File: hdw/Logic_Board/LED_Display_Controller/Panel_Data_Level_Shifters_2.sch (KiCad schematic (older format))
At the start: 62 parts, among them U2701 74HCT541, U2702 74HCT541

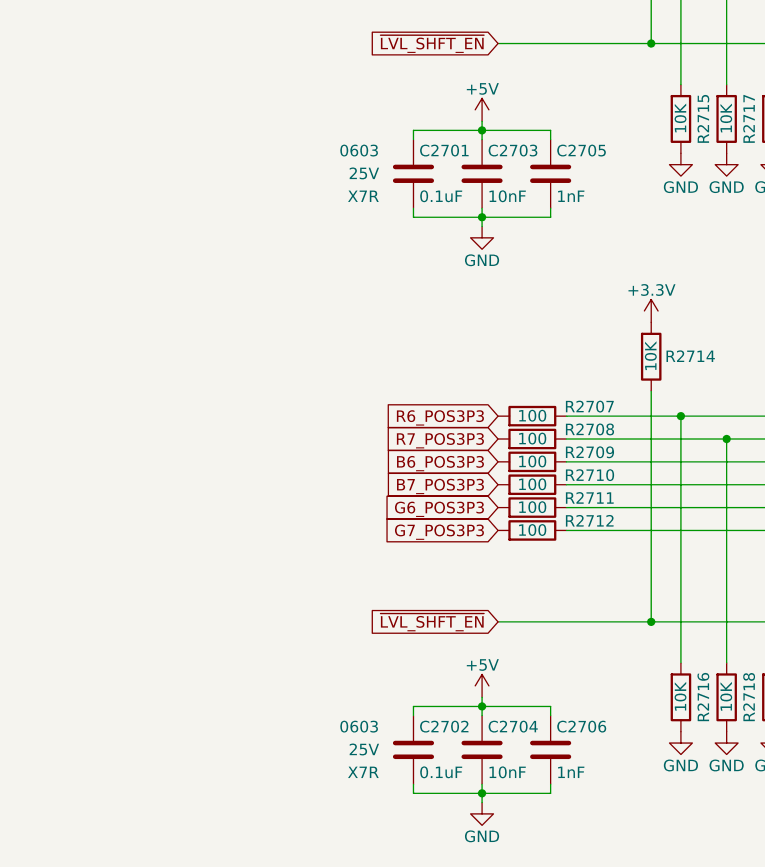
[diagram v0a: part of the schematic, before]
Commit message: Added some digikey partnumbers to components
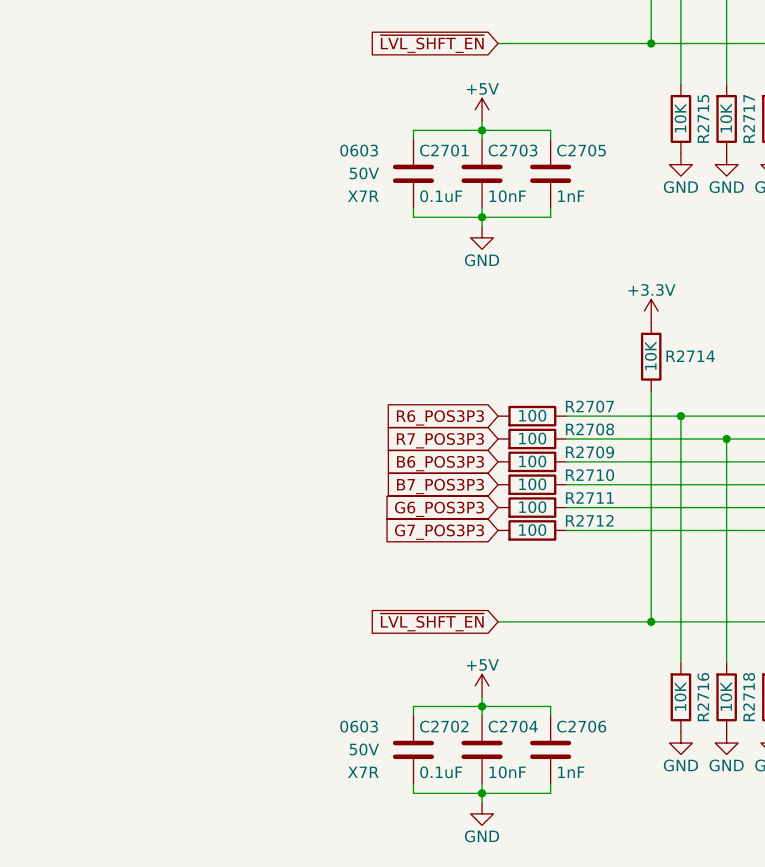
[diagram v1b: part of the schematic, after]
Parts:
- C2701, C2702: footprint (none) -> Capacitors_SMD:C_0603; Digi-Key PN PN -> 311-1344-1-ND; Voltage 25V -> 50V
- C2703, C2704: Digi-Key PN PN -> 1276-1921-1-ND; Voltage 25V -> 50V
- C2705, C2706: Digi-Key PN PN -> 1276-1018-1-ND; Voltage 25V -> 50V
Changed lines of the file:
@@
 F 0 "C2701" H 2305 3290 50  0000 L CNN
 F 1 "0.1uF" H 2305 3090 50  0000 L CNN
-F 2 "" H 2318 3040 50  0001 C CNN
+F 2 "Capacitors_SMD:C_0603" H 2318 3040 50  0001 C CNN
 F 3 "" H 2305 3290 50  0001 C CNN
 F 4 "0603" H 2130 3290 50  0000 R CNN "display_footprint"
-F 5 "25V" H 2130 3190 50  0000 R CNN "Voltage"
+F 5 "50V" H 2130 3190 50  0000 R CNN "Voltage"
 F 6 "X7R" H 2130 3090 50  0000 R CNN "Dielectric"
-F 7 "PN" H 2705 3690 60  0001 C CNN "Digi-Key PN"
+F 7 "311-1344-1-ND" H 2705 3690 60  0001 C CNN "Digi-Key PN"
 	1    2280 3190
 	1    0    0    -1
@@
 F 3 "" H 2605 3290 50  0001 C CNN
 F 4 "0603" H 2430 3290 50  0001 R CNN "display_footprint"
-F 5 "25V" H 2430 3190 50  0001 R CNN "Voltage"
+F 5 "50V" H 2430 3190 50  0001 R CNN "Voltage"
 F 6 "X7R" H 2430 3090 50  0001 R CNN "Dielectric"
-F 7 "PN" H 3005 3690 60  0001 C CNN "Digi-Key PN"
+F 7 "1276-1921-1-ND" H 3005 3690 60  0001 C CNN "Digi-Key PN"
 	1    2580 3190
 	1    0    0    -1
@@
 F 3 "" H 2905 3290 50  0001 C CNN
 F 4 "0603" H 2730 3290 50  0001 R CNN "display_footprint"
-F 5 "25V" H 2730 3190 50  0001 R CNN "Voltage"
+F 5 "50V" H 2730 3190 50  0001 R CNN "Voltage"
 F 6 "X7R" H 2730 3090 50  0001 R CNN "Dielectric"
-F 7 "PN" H 3305 3690 60  0001 C CNN "Digi-Key PN"
+F 7 "1276-1018-1-ND" H 3305 3690 60  0001 C CNN "Digi-Key PN"
 	1    2880 3190
 	1    0    0    -1
@@
 F 0 "C2702" H 2305 5810 50  0000 L CNN
 F 1 "0.1uF" H 2305 5610 50  0000 L CNN
-F 2 "" H 2318 5560 50  0001 C CNN
+F 2 "Capacitors_SMD:C_0603" H 2318 5560 50  0001 C CNN
 F 3 "" H 2305 5810 50  0001 C CNN
 F 4 "0603" H 2130 5810 50  0000 R CNN "display_footprint"
-F 5 "25V" H 2130 5710 50  0000 R CNN "Voltage"
+F 5 "50V" H 2130 5710 50  0000 R CNN "Voltage"
 F 6 "X7R" H 2130 5610 50  0000 R CNN "Dielectric"
-F 7 "PN" H 2705 6210 60  0001 C CNN "Digi-Key PN"
+F 7 "311-1344-1-ND" H 2705 6210 60  0001 C CNN "Digi-Key PN"
 	1    2280 5710
 	1    0    0    -1
@@
 F 3 "" H 2605 5810 50  0001 C CNN
 F 4 "0603" H 2430 5810 50  0001 R CNN "display_footprint"
-F 5 "25V" H 2430 5710 50  0001 R CNN "Voltage"
+F 5 "50V" H 2430 5710 50  0001 R CNN "Voltage"
 F 6 "X7R" H 2430 5610 50  0001 R CNN "Dielectric"
-F 7 "PN" H 3005 6210 60  0001 C CNN "Digi-Key PN"
+F 7 "1276-1921-1-ND" H 3005 6210 60  0001 C CNN "Digi-Key PN"
 	1    2580 5710
 	1    0    0    -1
@@
 F 3 "" H 2905 5810 50  0001 C CNN
 F 4 "0603" H 2730 5810 50  0001 R CNN "display_footprint"
-F 5 "25V" H 2730 5710 50  0001 R CNN "Voltage"
+F 5 "50V" H 2730 5710 50  0001 R CNN "Voltage"
 F 6 "X7R" H 2730 5610 50  0001 R CNN "Dielectric"
-F 7 "PN" H 3305 6210 60  0001 C CNN "Digi-Key PN"
+F 7 "1276-1018-1-ND" H 3305 6210 60  0001 C CNN "Digi-Key PN"
 	1    2880 5710
 	1    0    0    -1

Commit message: Finished first pass of digikey part numbers
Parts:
- R2701, R2702, R2703, R2704, R2705, R2706, R2707, R2708, R2709, R2710, R2711, R2712, R2743, R2744, R2745, R2746, R2747, R2748, R2749, R2750, R2751, R2752, R2753, R2754: Digi-Key PN PN -> A106047CT-ND
- R2713, R2714, R2715, R2716, R2717, R2718, R2719, R2720, R2721, R2722, R2723, R2724, R2725, R2726, R2727, R2728, R2729, R2730, R2731, R2732, R2733, R2734, R2735, R2736, R2737, R2738, R2739, R2740, R2741, R2742: Digi-Key PN PN -> RMCF0603FT10K0CT-ND
- U2701, U2702: Digi-Key PN (none) -> 296-26499-1-ND

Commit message: First pass assignment of footprints to all components
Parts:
- C2703, C2704, C2705, C2706: footprint (none) -> Capacitors_SMD:C_0603
- R2701, R2702, R2703, R2704, R2705, R2706, R2707, R2708, R2709, R2710, R2711, R2712, R2713, R2714, R2715, R2716, R2717, R2718, R2719, R2720, R2721, R2722, R2723, R2724, R2725, R2726, R2727, R2728, R2729, R2730, R2731, R2732, R2733, R2734, R2735, R2736, R2737, R2738, R2739, R2740, R2741, R2742, R2743, R2744, R2745, R2746, R2747, R2748, R2749, R2750, R2751, R2752, R2753, R2754: footprint (none) -> Resistors_SMD:R_0603
- U2701, U2702: footprint (none) -> Housings_SSOP:TSSOP-20_4.4x6.5mm_Pitch0.65mm

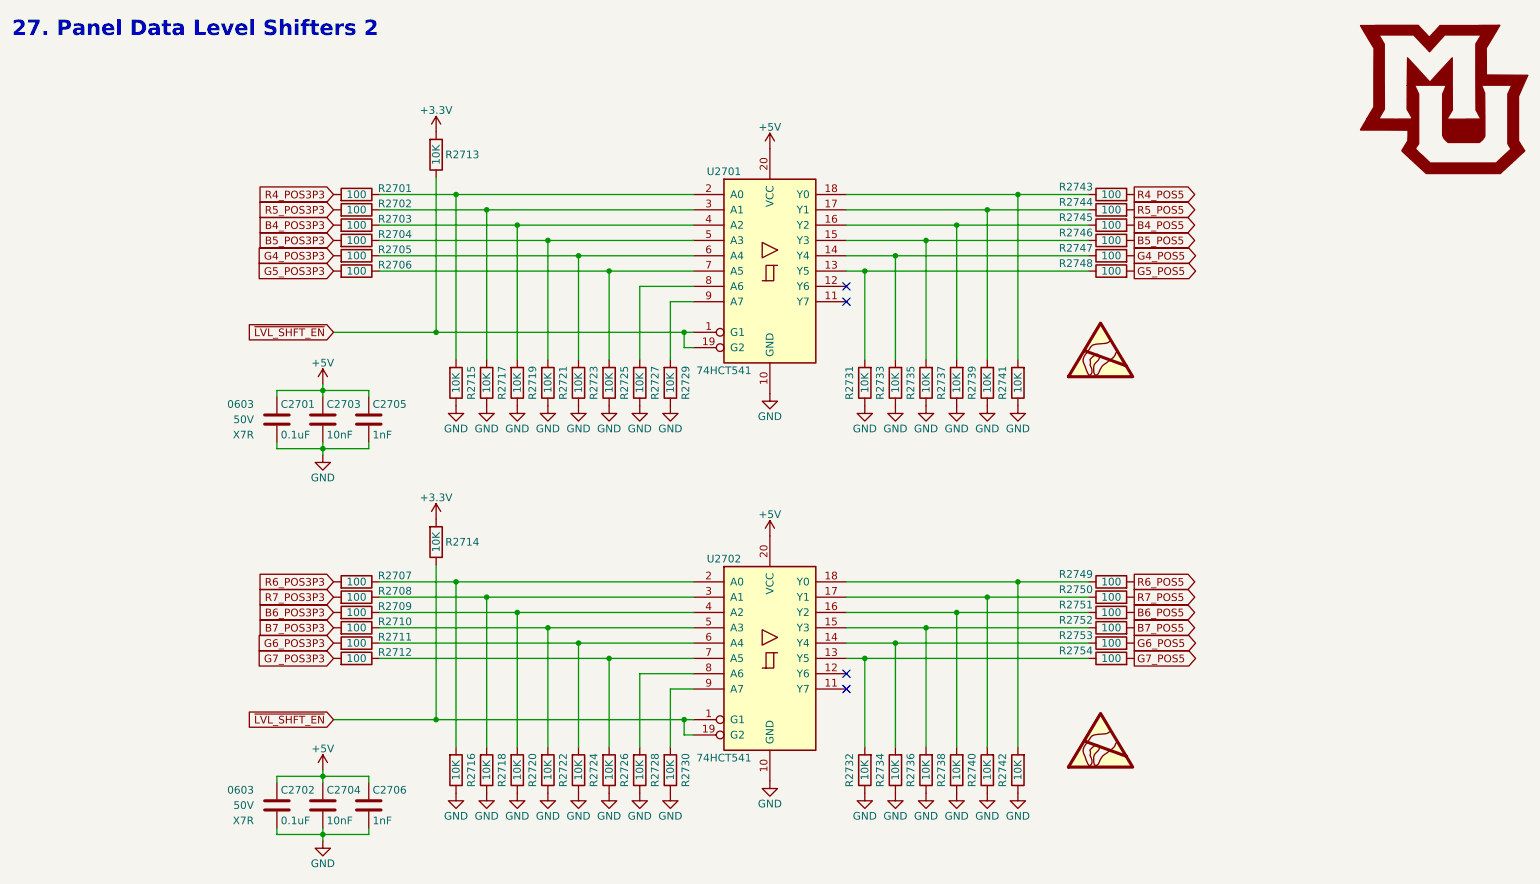
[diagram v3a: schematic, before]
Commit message: Fixed net placement on level shifters, lots of part placements on PCB
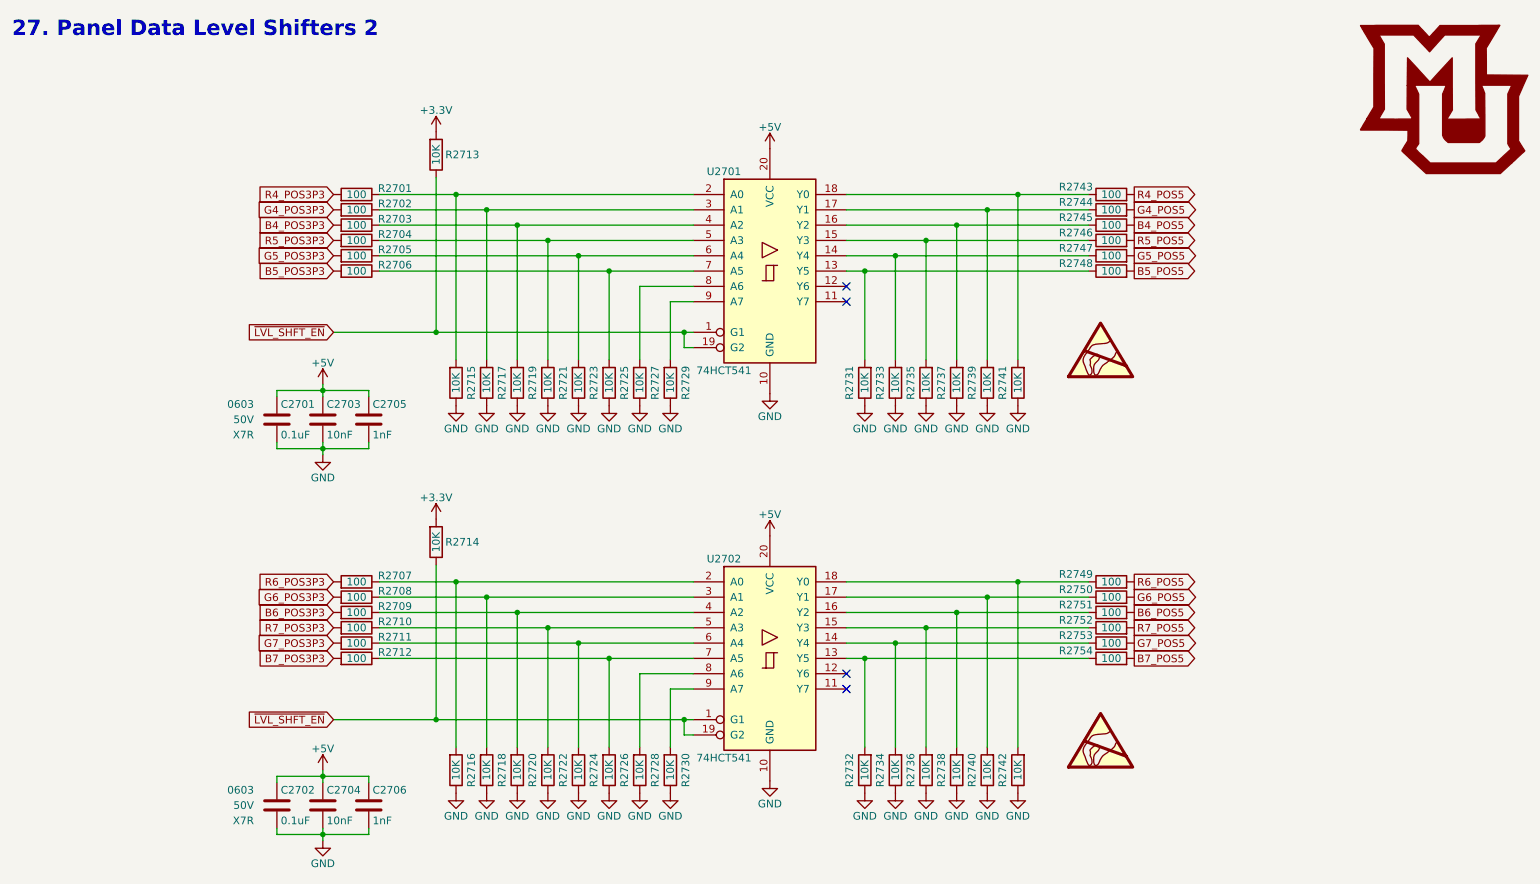
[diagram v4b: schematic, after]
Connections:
- net B5_POS3P3: now also R2706.1; no longer R2704.1
- net B5_POS5: now also R2748.1; no longer R2746.1
- net B7_POS3P3: now also R2712.1; no longer R2710.1
- net B7_POS5: now also R2754.1; no longer R2752.1
- net G4_POS3P3: now also R2702.1; no longer R2705.1
- net G4_POS5: now also R2744.1; no longer R2747.1
- net G5_POS3P3: now also R2705.1; no longer R2706.1
- net G5_POS5: now also R2747.1; no longer R2748.1
- net G6_POS3P3: now also R2708.1; no longer R2711.1
- net G6_POS5: now also R2750.1; no longer R2753.1
- net G7_POS3P3: now also R2711.1; no longer R2712.1
- net G7_POS5: now also R2753.1; no longer R2754.1
- net R5_POS3P3: now also R2704.1; no longer R2702.1
- net R5_POS5: now also R2746.1; no longer R2744.1
- net R7_POS3P3: now also R2710.1; no longer R2708.1
- net R7_POS5: now also R2752.1; no longer R2750.1
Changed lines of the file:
@@
 Text GLabel 7880 1720 2    50   Output ~ 0
 R4_POS5
-Text GLabel 7880 1820 2    50   Output ~ 0
+Text GLabel 7880 2020 2    50   Output ~ 0
 R5_POS5
 Text GLabel 7880 1920 2    50   Output ~ 0
 B4_POS5
-Text GLabel 7880 2020 2    50   Output ~ 0
+Text GLabel 7880 2220 2    50   Output ~ 0
 B5_POS5
+Text GLabel 7880 1820 2    50   Output ~ 0
+G4_POS5
 Text GLabel 7880 2120 2    50   Output ~ 0
-G4_POS5
-Text GLabel 7880 2220 2    50   Output ~ 0
 G5_POS5
 $Comp
@@
 Text GLabel 2650 1720 0    50   Input ~ 0
 R4_POS3P3
-Text GLabel 2650 1820 0    50   Input ~ 0
+Text GLabel 2650 2020 0    50   Input ~ 0
 R5_POS3P3
 Text GLabel 2650 1920 0    50   Input ~ 0
 B4_POS3P3
-Text GLabel 2650 2020 0    50   Input ~ 0
+Text GLabel 2650 2220 0    50   Input ~ 0
 B5_POS3P3
+Text GLabel 2650 1820 0    50   Input ~ 0
+G4_POS3P3
 Text GLabel 2650 2120 0    50   Input ~ 0
-G4_POS3P3
-Text GLabel 2650 2220 0    50   Input ~ 0
 G5_POS3P3
 Wire Wire Line
@@
 Text GLabel 7880 4250 2    50   Output ~ 0
 R6_POS5
-Text GLabel 7880 4350 2    50   Output ~ 0
+Text GLabel 7880 4550 2    50   Output ~ 0
 R7_POS5
 Text GLabel 7880 4450 2    50   Output ~ 0
 B6_POS5
-Text GLabel 7880 4550 2    50   Output ~ 0
+Text GLabel 7880 4750 2    50   Output ~ 0
 B7_POS5
+Text GLabel 7880 4350 2    50   Output ~ 0
+G6_POS5
 Text GLabel 7880 4650 2    50   Output ~ 0
-G6_POS5
-Text GLabel 7880 4750 2    50   Output ~ 0
 G7_POS5
 $Comp
@@
 Text GLabel 2650 4250 0    50   Input ~ 0
 R6_POS3P3
-Text GLabel 2650 4350 0    50   Input ~ 0
+Text GLabel 2650 4550 0    50   Input ~ 0
 R7_POS3P3
 Text GLabel 2650 4450 0    50   Input ~ 0
 B6_POS3P3
-Text GLabel 2650 4550 0    50   Input ~ 0
+Text GLabel 2650 4750 0    50   Input ~ 0
 B7_POS3P3
+Text GLabel 2650 4350 0    50   Input ~ 0
+G6_POS3P3
 Text GLabel 2650 4650 0    50   Input ~ 0
-G6_POS3P3
-Text GLabel 2650 4750 0    50   Input ~ 0
 G7_POS3P3
 Wire Wire Line
